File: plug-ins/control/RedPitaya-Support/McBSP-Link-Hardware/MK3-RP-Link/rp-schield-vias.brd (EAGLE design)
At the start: 59.4 x 51.2 mm, 16 parts, among them U1 SN65MLVD202A, U2 SN65MLVD202A, U3 SN65MLVD202A

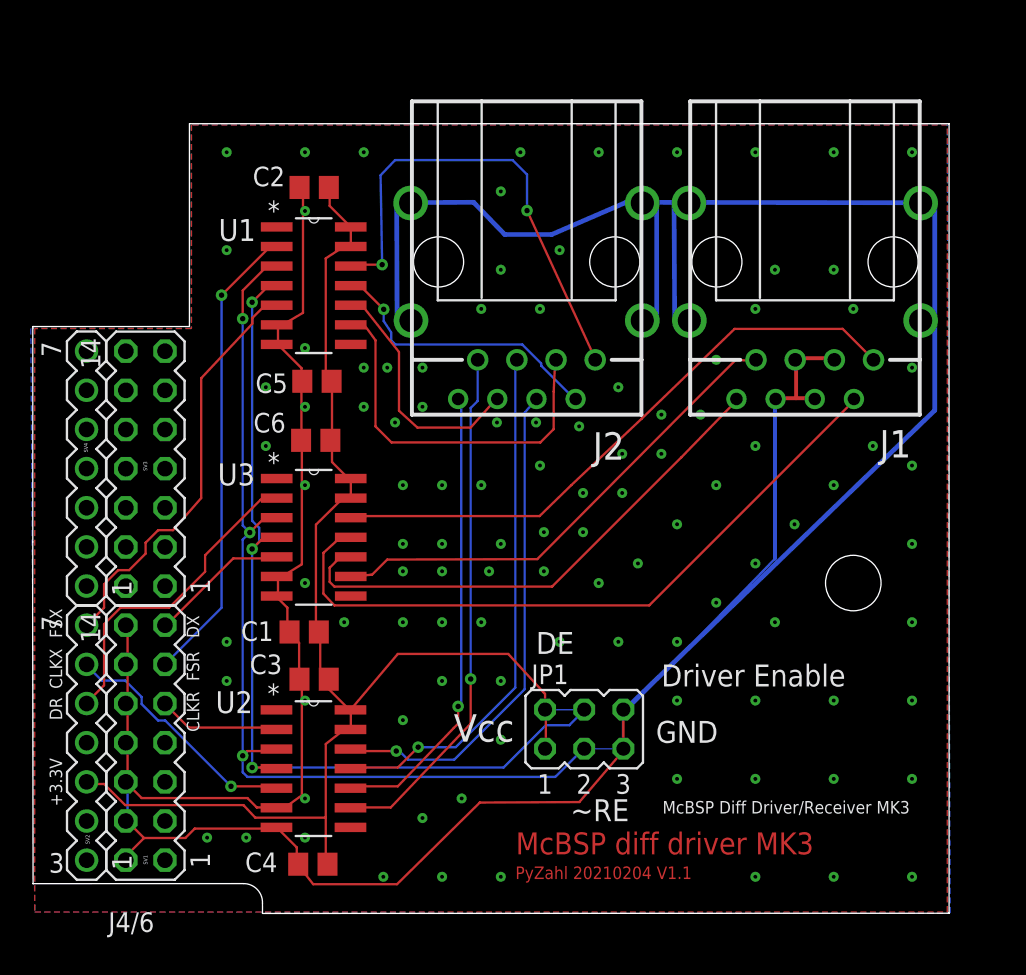
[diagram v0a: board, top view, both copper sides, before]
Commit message: added next version and support material
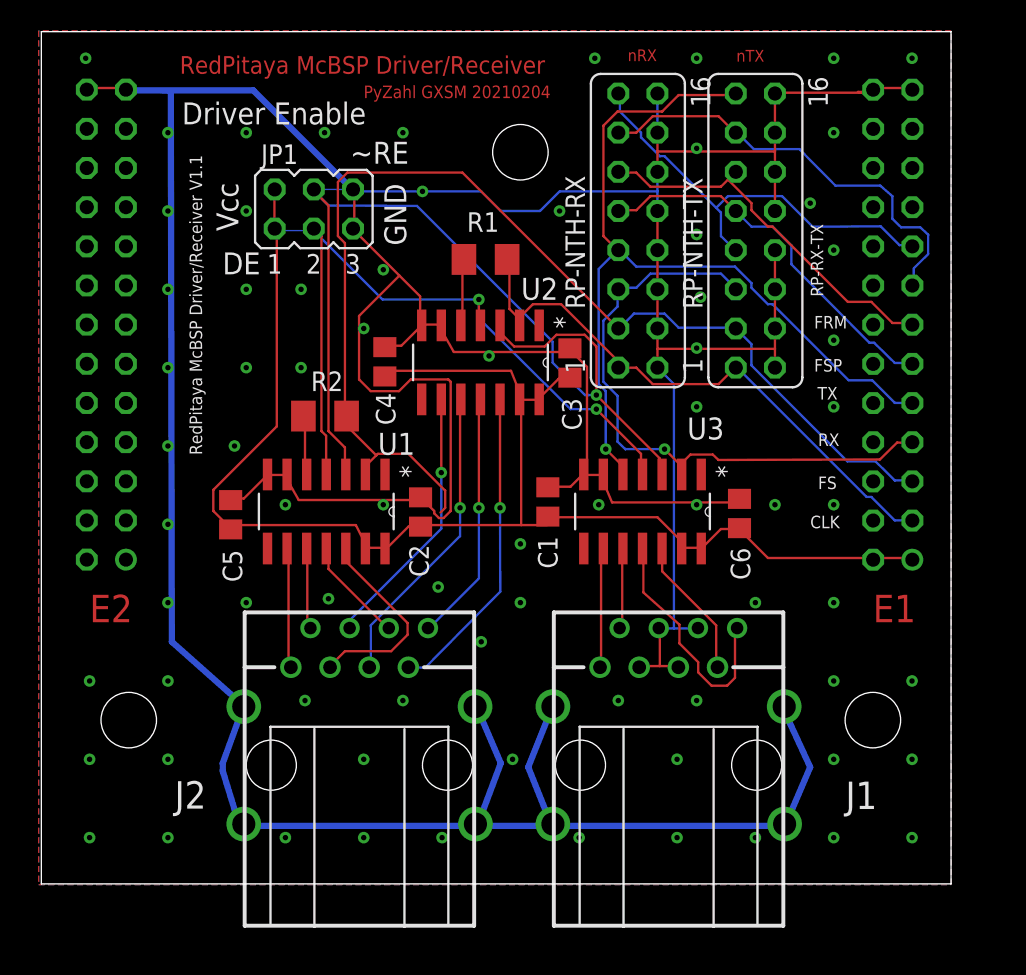
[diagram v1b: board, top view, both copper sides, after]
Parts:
- removed SV1, SV3: J4, con-lstb:MA07-2
- removed SV2, SV4: (no value), con-lstb-copy:MA07-1
- added R1, R2: 24R9, resistor:M1206
- added RP-E1, RP-E2: (no value), con-lsta:FE13-2
- added RP-NTH-RX, RP-NTH-TX: (no value), con-lsta:FE08-2
- moved JP1 38.0 mm to (19.6, 48.4)
- moved J2 34.4 mm to (22.6, 12.3), turned to 0 degrees
- moved J1 33.8 mm to (42.6, 12.3), turned to 0 degrees
- moved C4 32.9 mm to (24.2, 38.5), turned to 270 degrees
- moved U2 28.1 mm to (26.6, 36.0), turned to 270 degrees
- moved C6 27.9 mm to (47.2, 28.6), turned to 270 degrees
- moved C3 26.4 mm to (36.2, 38.4), turned to 270 degrees
- moved C2 22.1 mm to (26.5, 28.7), turned to 270 degrees
- moved C1 17.9 mm to (34.8, 29.4), turned to 270 degrees
- moved U3 15.4 mm to (37.1, 26.4), turned to 270 degrees
- moved U1 14.3 mm to (16.6, 26.4), turned to 270 degrees
- moved C5 10.3 mm to (14.2, 28.6), turned to 270 degrees
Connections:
- removed net CLKR0: SV1.9, U2.2
- removed net CLKX0: SV2.6, U2.5
- removed net DR0: SV2.5, U3.2
- removed net DX0: SV1.13, U3.5
- removed net FSR0: SV1.11, U1.2
- removed net FSX0: SV2.7, U1.5
- removed net N$1: J1.1, U3.12
- removed net N$11: J2.7, U2.9
- removed net N$12: J2.8, U2.10
- removed net N$3: J1.7, U3.9
- removed net N$4: J1.8, U3.10
- removed net N$5: J2.1, U1.12
- removed net N$7: J2.3, U1.9
- removed net N$8: J2.6, U1.10
- removed net N$9: J2.4, U2.12
- new net CLK+-CLKX: J2.4, U2.9
- new net CLK+RET-CLKR: J2.7, U2.12
- new net CLK--CLKX: J2.5, U2.10
- new net CLK-RET-CLKR: J2.8, U2.11
- new net CS+-FSX: J2.3, U1.12
- new net CS+RET-FSR: J2.1, U1.9
- new net CS-FSX: J2.6, U1.11
- new net CS-RET-FSR: J2.2, U1.10
- new net FPGA-S-CLK: R1.1, RP-E1.3, RP-NTH-RX.1, RP-NTH-TX.1, U2.2
- new net FPGA-S-FS: R2.1, RP-E1.5, RP-NTH-RX.3, RP-NTH-TX.3, U1.2
- new net FPGA-S-RX: RP-E1.7, RP-NTH-RX.5, RP-NTH-TX.5, U3.2
- new net FPGA-S-TX: RP-E1.9, RP-NTH-RX.7, RP-NTH-TX.15, U3.5
- new net FRM: RP-E1.13, RP-NTH-RX.11, RP-NTH-TX.11
- new net FSP: RP-E1.11, RP-NTH-RX.9, RP-NTH-TX.9
- new net MISO+: J1.1, U3.9
- new net MISO-: J1.2, U3.10
- new net MOSI+: J1.7, U3.12
- new net MOSI-: J1.8, U3.11
- new net RP-RX-TX-CHAIN: RP-E1.17, RP-NTH-RX.15, RP-NTH-TX.7
- net DE: now also JP1.3; no longer JP1.4
- net GND: now also RP-E1.25, RP-E1.26, RP-E2.25, RP-E2.26, RP-NTH-RX.10, RP-NTH-RX.12, RP-NTH-RX.14, RP-NTH-RX.16, RP-NTH-RX.2, RP-NTH-RX.4, RP-NTH-RX.6, RP-NTH-RX.8, RP-NTH-TX.10, RP-NTH-TX.12, RP-NTH-TX.14, RP-NTH-TX.16, RP-NTH-TX.2, RP-NTH-TX.4, RP-NTH-TX.6, RP-NTH-TX.8; no longer SV1.10, SV1.12, SV1.14, SV1.2, SV1.4, SV1.6, SV1.8
- net N$10: now also RP-E1.15, RP-NTH-RX.13, RP-NTH-TX.13; no longer J2.5, U2.11
- net N$2: now also R1.2, U2.5; no longer J1.2, U3.11
- net N$6: now also R2.2, U1.5; no longer J2.2, U1.11
- net VCC+3.3V: now also RP-E1.1, RP-E1.2; no longer SV2.3
- net ~RE: now also JP1.4; no longer JP1.3
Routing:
- net GND: track 253.3 -> 328.1 mm, vias 0 -> 75
- net FPGA-S-FS: track 0.00 -> 74.7 mm
- net FPGA-S-TX: track 0.00 -> 57.1 mm, vias 0 -> 1
- net FPGA-S-RX: track 0.00 -> 41.0 mm, vias 0 -> 1
- net N$2: track 45.3 -> 4.97 mm
- net N$1: track 39.7 -> 0.00 mm
- net FPGA-S-CLK: track 0.00 -> 38.1 mm
- net N$4: track 34.3 -> 0.00 mm
- net N$11: track 33.9 -> 0.00 mm, vias 1 -> 0
- net N$9: track 32.6 -> 0.00 mm, vias 1 -> 0
- net N$3: track 32.1 -> 0.00 mm
- net N$5: track 31.2 -> 0.00 mm, vias 2 -> 0
- net FSR0: track 30.4 -> 0.00 mm, vias 1 -> 0
- net N$12: track 30.2 -> 0.00 mm, vias 1 -> 0
- net RP-RX-TX-CHAIN: track 0.00 -> 27.9 mm
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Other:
- board size 59.4 x 51.2 mm -> 59 x 55.3 mm
- board text added: "CLK"
- board text added: "E1"
- board text added: "E2"
- board text added: "FRM"
- board text added: "FS"
- board text added: "FSP"
- board text added: "PyZahl GXSM 20210204"
- board text added: "RP-RX-TX"
- board text added: "RX"
- board text added: "RedPitaya McBSP Driver/Receiver"
- board text added: "RedPitaya McBSP Driver/Receiver V1.1"
- board text added: "TX"
- board text added: "nRX"
- board text added: "nTX"
- board text removed: "+3.3V"
- board text removed: "3"
- board text removed: "CLKR"
- board text removed: "CLKX"
- board text removed: "DR"
- board text removed: "DX"
- board text removed: "FSR"
- board text removed: "FSX"
- board text removed: "J4/6"
- board text removed: "McBSP Diff Driver/Receiver MK3"
- board text removed: "McBSP diff driver MK3"
- board text removed: "PyZahl 20210204 V1.1"

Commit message: updated McBSP Link board/schematics updated FPGA bit file for (latest build for V2 Hardware/Interface), design cleanups
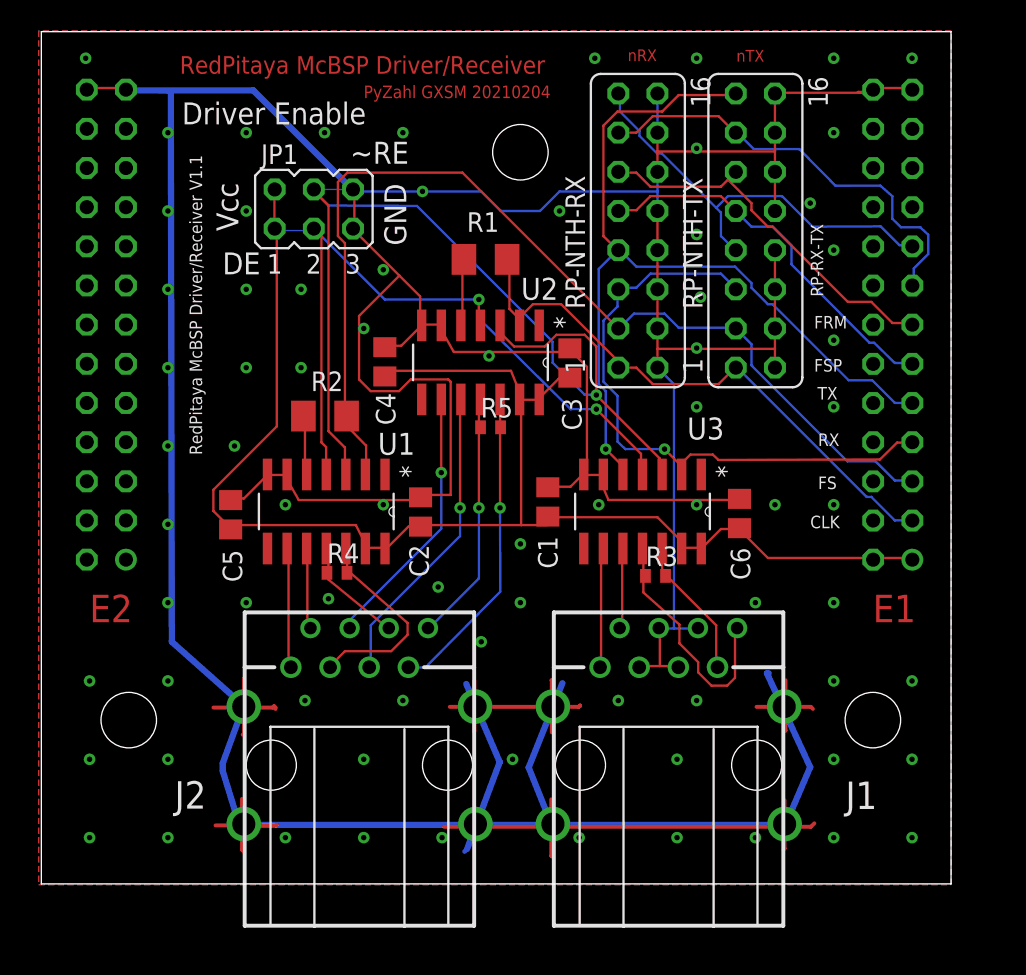
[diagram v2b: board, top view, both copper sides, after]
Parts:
- added R3, R4, R5: 100R, resistor:R0402
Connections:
- net CLK+RET-CLKR: now also R5.2
- net CLK-RET-CLKR: now also R5.1
- net CS+-FSX: now also R4.2
- net CS-FSX: now also R4.1
- net MOSI+: now also R3.2
- net MOSI-: now also R3.1
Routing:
- net GND: track 328.1 -> 402.3 mm
- net FPGA-S-FS: track 74.7 -> 67.1 mm
- net ~RE: track 62.7 -> 61.7 mm
- net FPGA-S-CLK: track 38.1 -> 37.2 mm

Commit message: minor updates, cleanups
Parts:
- moved R3 0.16 mm to (41.6, 24.7)
- moved R4 0.09 mm to (21.1, 24.7)
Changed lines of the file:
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@@
 <drawing>
 <settings>
-<setting alwaysvectorfont="no"/>
+<setting alwaysvectorfont="yes"/>
 <setting verticaltext="up"/>
 </settings>
@@
 <attribute name="VALUE" x="45.339" y="36.83" size="1.27" layer="27" ratio="10" rot="R90"/>
 </element>
-<element name="R3" library="resistor" library_urn="urn:adsk.eagle:library:348" package="R0402" package3d_urn="urn:adsk.eagle:package:26058/1" value="100R" x="41.7823125" y="24.594221875"/>
-<element name="R4" library="resistor" library_urn="urn:adsk.eagle:library:348" package="R0402" package3d_urn="urn:adsk.eagle:package:26058/1" value="100R" x="21.125246875" y="24.7952"/>
-<element name="R5" library="resistor" library_urn="urn:adsk.eagle:library:348" package="R0402" package3d_urn="urn:adsk.eagle:package:26058/1" value="100R" x="31.083778125" y="34.232609375"/>
+<element name="R3" library="resistor" library_urn="urn:adsk.eagle:library:348" package="R0402" package3d_urn="urn:adsk.eagle:package:26058/1" value="100R" x="41.6412375" y="24.671178125"/>
+<element name="R4" library="resistor" library_urn="urn:adsk.eagle:library:348" package="R0402" package3d_urn="urn:adsk.eagle:package:26058/1" value="100R" x="21.1160125" y="24.7075625"/>
+<element name="R5" library="resistor" library_urn="urn:adsk.eagle:library:348" package="R0402" package3d_urn="urn:adsk.eagle:package:26058/1" value="100R" x="31.058128125" y="34.258259375"/>
 </elements>
 <signals>
@@
 <wire x1="45.72" y1="18.796" x2="45.805" y2="18.67" width="0.1524" layer="1"/>
 <contactref element="R3" pad="2"/>
-<wire x1="42.4323125" y1="24.594221875" x2="42.2148" y2="24.892" width="0" layer="19" extent="1-1"/>
+<wire x1="42.2912375" y1="24.671178125" x2="42.2148" y2="24.892" width="0" layer="19" extent="1-1"/>
 </signal>
 <signal name="MOSI-">
@@
 <wire x1="46.9392" y1="21.082" x2="47.075" y2="21.21" width="0.1524" layer="1"/>
 <contactref element="R3" pad="1"/>
-<wire x1="40.9956" y1="23.5204" x2="41.1323125" y2="24.594221875" width="0" layer="19" extent="1-1"/>
+<wire x1="40.9956" y1="23.5204" x2="40.9912375" y2="24.671178125" width="0" layer="19" extent="1-1"/>
 </signal>
 <signal name="CS+RET-FSR">
@@
 <wire x1="20.7264" y1="18.796" x2="20.675" y2="18.67" width="0.1524" layer="1"/>
 <contactref element="R4" pad="2"/>
-<wire x1="21.776109375" y1="24.989340625" x2="21.775246875" y2="24.7952" width="0" layer="19" extent="1-1"/>
+<wire x1="21.776109375" y1="24.989340625" x2="21.7660125" y2="24.7075625" width="0" layer="19" extent="1-1"/>
 </signal>
 <signal name="CS-FSX">
@@
 <wire x1="24.384" y1="21.2344" x2="24.485" y2="21.21" width="0.1524" layer="1"/>
 <contactref element="R4" pad="1"/>
-<wire x1="20.475246875" y1="24.7952" x2="20.56545625" y2="24.36075625" width="0" layer="19" extent="1-1"/>
+<wire x1="20.4660125" y1="24.7075625" x2="20.56545625" y2="24.36075625" width="0" layer="19" extent="1-1"/>
 </signal>
 <signal name="CLK+-CLKX">
@@
 <via x="31.6992" y="29.0068" extent="1-16" drill="0.35"/>
 <contactref element="R5" pad="2"/>
-<wire x1="31.6992" y1="36.0172" x2="31.733778125" y2="34.232609375" width="0" layer="19" extent="1-1"/>
+<wire x1="31.6992" y1="36.0172" x2="31.708128125" y2="34.258259375" width="0" layer="19" extent="1-1"/>
 </signal>
 <signal name="CLK-RET-CLKR">
@@
 <via x="30.3276" y="29.0068" extent="1-16" drill="0.35"/>
 <contactref element="R5" pad="1"/>
-<wire x1="30.3276" y1="36.0172" x2="30.433778125" y2="34.232609375" width="0" layer="19" extent="1-1"/>
+<wire x1="30.3276" y1="36.0172" x2="30.408128125" y2="34.258259375" width="0" layer="19" extent="1-1"/>
 </signal>
 <signal name="~RE">

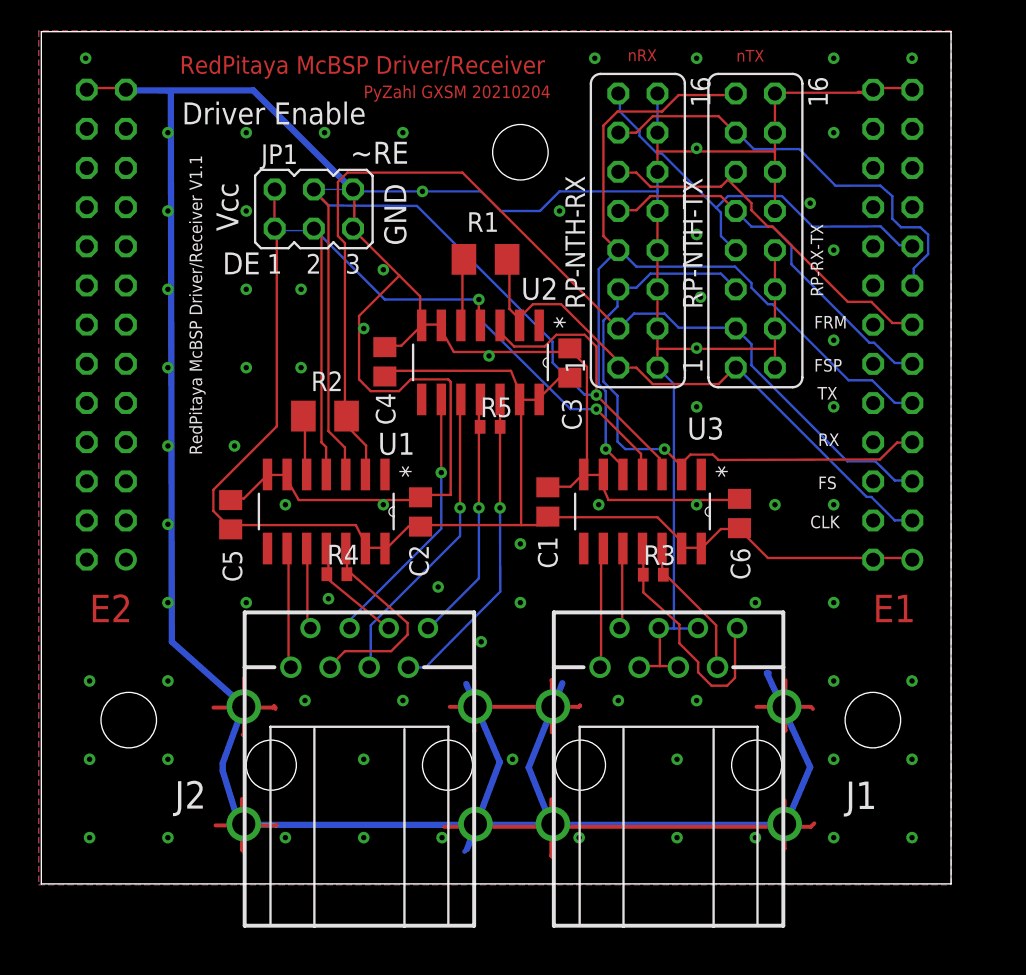
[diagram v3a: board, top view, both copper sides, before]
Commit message: updated FPGA init procedure updated -- next gen layout
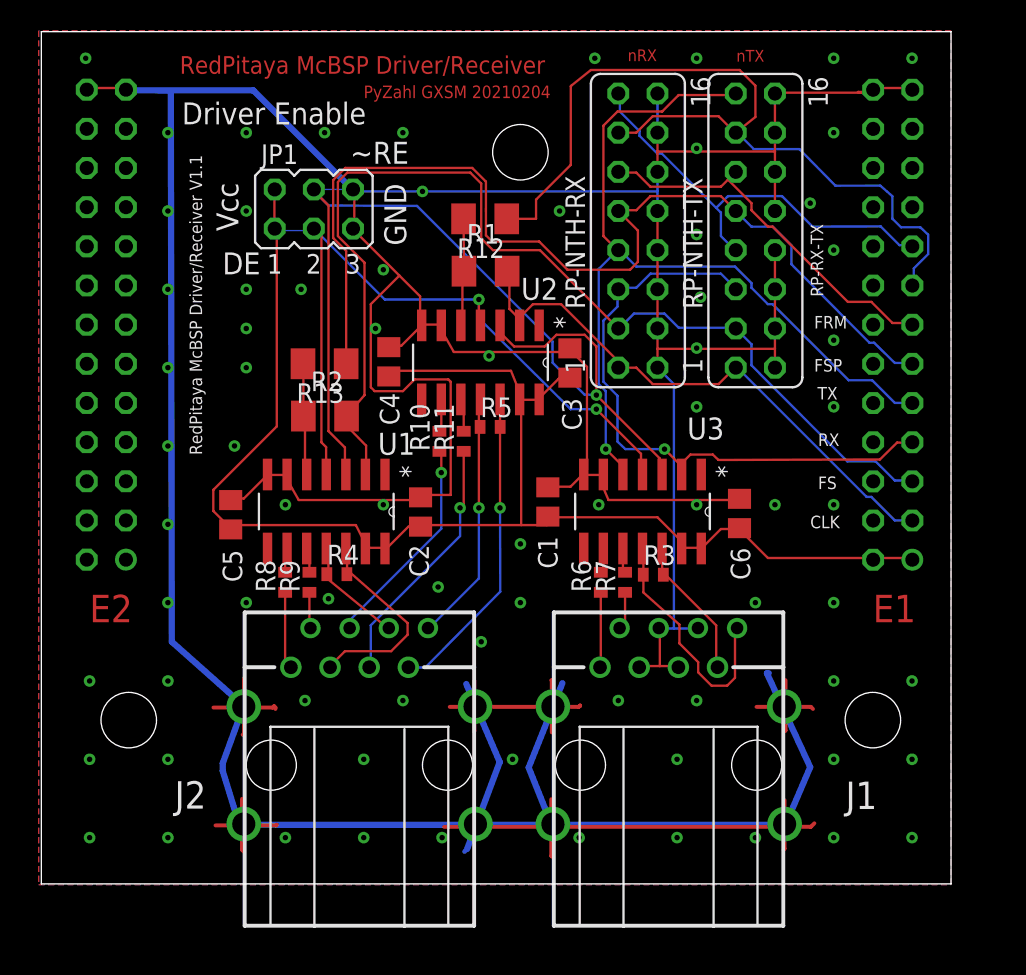
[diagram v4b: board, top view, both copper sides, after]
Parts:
- added R10, R11, R6, R7, R8, R9: 25R, resistor:R0402
- added R12, R13: 0R, resistor:M1206
- R1, R2: value 24R9 -> XXR
- moved R1 0.76 mm to (30.8, 44.4)
- moved C4 0.25 mm to (24.5, 38.5)
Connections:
- net FPGA-S-CLK renamed CLKX
- new net N$1: R6.2, U3.9
- new net N$3: R7.2, U3.10
- new net N$4: R8.2, U1.9
- new net N$5: R9.2, U1.10
- new net N$7: R10.2, U2.9
- new net N$8: R11.2, U2.10
- net CLK+-CLKX: now also R10.1; no longer U2.9
- net CLK--CLKX: now also R11.1; no longer U2.10
- net CS+RET-FSR: now also R8.1; no longer U1.9
- net CS-RET-FSR: now also R9.1; no longer U1.10
- net FSP: now also R13.1
- net MISO+: now also R6.1; no longer U3.9
- net MISO-: now also R7.1; no longer U3.10
- net N$10: now also R12.1
- net N$2: now also R12.2
- net N$6: now also R13.2
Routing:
- net FSP: track 24.7 -> 65.8 mm
- net N$10: track 28.3 -> 56.2 mm
- net N$2: track 4.92 -> 8.97 mm
- net N$6: track 3.91 -> 7.31 mm
- net CLK+-CLKX: track 17.3 -> 14.0 mm
- net CLK--CLKX: track 19.8 -> 16.5 mm
- net FPGA-S-FS: track 67.1 -> 70.1 mm
- net MISO+: track 7.79 -> 4.88 mm
- net CS-RET-FSR: track 5.26 -> 2.62 mm
- net CS+RET-FSR: track 7.81 -> 5.21 mm
- net MISO-: track 5.24 -> 2.71 mm
- net N$8: track 0.00 -> 2.15 mm
- net N$7: track 0.00 -> 2.12 mm
- net GND: track 402.3 -> 400.6 mm
- net N$5: track 0.00 -> 1.62 mm
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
